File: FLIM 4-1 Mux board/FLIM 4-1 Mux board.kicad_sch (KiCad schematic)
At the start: 17 parts, among them U1 PTMUX8109PWR, U2 DI79L18UAB, U3 DI78L18UAB

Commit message: Add buttons
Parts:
- added J1, J2: Conn_01x14_Pin, symbol Connector:Conn_01x14_Pin
- added J3: Conn_01x05_Pin, symbol Connector:Conn_01x05_Pin
- added R3: 1k, Resistor_SMD:R_0805_2012Metric, symbol Device:R
- added SW1: SW_Push_LED, Custom:TSSLE 6868 R RNN J, symbol Switch:SW_Push_LED
- added U4: Itsy_Bitsy_32u4, Custom:Itsy Bitsy 32u4 with headers, symbol custom:Itsy_Bitsy_32u4
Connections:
- net GND: now also J1.4 (Pin_4), J2.2 (Pin_2), J3.2 (Pin_2), SW1.1, SW1.3 (K), U4.16 (Gnd), U4.32 (Gnd), U4.4 (GND)
- new net: R3.1, SW1.4 (A)
- new net 3v3: J1.14 (Pin_14), U4.14 (3.3V)
- new net 5V: J1.2 (Pin_2), U4.2 (5V)
- no-connect marks 0 -> 10

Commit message: Last update before change to cascade RF switches
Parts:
- added R4, R5, R6: 1k, Resistor_SMD:R_0805_2012Metric, symbol Device:R
- added SW2, SW3, SW4: SW_Push_LED, Custom:TSSLE 6868 R RNN J, symbol Switch:SW_Push_LED
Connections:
- net GND: now also SW2.1, SW2.3 (K), SW3.1, SW3.3 (K), SW4.1, SW4.3 (K)
- new net: R4.1, SW2.4 (A)
- new net: R5.1, SW3.4 (A)
- new net: R6.1, SW4.4 (A)
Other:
- moved on the sheet: R3, SW1

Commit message: Working draft of full setup
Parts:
- removed PS1: PDSE1-S24-D24-M, PDSE1-S24-D24-M:CONV_PDSE1-S24-D24-M, symbol Custom:PDSE1-S24-D24-M
- removed R1, R2, R3, R4, R5, R6: 1k, Resistor_SMD:R_0805_2012Metric, symbol Device:R
- removed U1: PTMUX8109PWR, TSSOP_8109PWR_TEX, symbol Custom:PTMUX8109PWR
- removed U2: DI79L18UAB, Package_TO_SOT_SMD:SOT-89-3, symbol Regulator_Linear:MCP1703Ax-150xxMB
- removed U3: DI78L18UAB, Package_TO_SOT_SMD:SOT-89-3, symbol Regulator_Linear:MCP1804x-1802xDB
- added C12, C13, C14: 8.2 nF, Capacitor_SMD:C_0402_1005Metric, symbol Device:C_Small
- added C15, C16, C17, C18, C19, C20: 100 pF, Capacitor_SMD:C_0603_1608Metric, symbol Device:C_Small
- added C21, C22, C23, C24: 1 µF, Capacitor_SMD:C_0603_1608Metric, symbol Device:C_Small
- added J10, J11, J12, J13: Conn_01x03_Socket, Connector_PinSocket_2.54mm:PinSocket_1x03_P2.54mm_Vertical_SMD_Pin1Left, symbol Connector:Conn_01x03_Socket
- added J14, J15, J16, J17: Conn_01x03_Pin, symbol Connector:Conn_01x03_Pin
- added J4, J5, J6, J7, J8: Conn_Coaxial, Custom:60312242114510, symbol Connector:Conn_Coaxial
- added J9: Barrel_Jack, Custom:CONN4_00165_TEN, symbol Connector:Barrel_Jack
- added R1, R10, R11, R12, R2, R3, R4, R5, R6, R7, R8, R9: 1k, Resistor_SMD:R_0603_1608Metric, symbol Device:R_Small
- added U1, U5, U6: SPDT RF switch, Custom:MSOP8G_8_ADI, symbol Custom:HMC284AMS8GETR
- added U2: CD74HCT175M96, Custom:74HCT175, symbol Custom:CD74HCT175M96
- added U3: ADM7150ARDZ-5.0, Custom:ADM7150ARDZ-5, symbol Custom:ADM7150ARDZ-5.0
- C1, C3: value 10µF -> 8.2 nF; footprint Capacitor_SMD:C_0805_2012Metric -> Capacitor_SMD:C_0402_1005Metric; Manufacturer Cal-Chip Electronics, Inc. -> Murata Electronics; Part # GMC21X5R106K50NT -> GRM1555C1H822GE01D
- C10, C11: value 100nF -> 1 µF; footprint Capacitor_SMD:C_0805_2012Metric -> Capacitor_SMD:C_0603_1608Metric; Manufacturer Cal-Chip Electronics, Inc. -> Walsin Technology Corporation; Part # GMC21X7R104M100NT -> 0603B105K250CT
- C2, C4: value 100nF -> 8.2 nF; footprint Capacitor_SMD:C_0805_2012Metric -> Capacitor_SMD:C_0402_1005Metric; Manufacturer Cal-Chip Electronics, Inc. -> Murata Electronics; Part # GMC21X7R104M100NT -> GRM1555C1H822GE01D
- C5: value 4.7µF -> 10 µF; footprint Capacitor_SMD:C_0805_2012Metric -> Capacitor_SMD:C_1210_3225Metric; Manufacturer Murata Electronics -> Walsin Technology Corporation; Part # GRM21BR71C475KE51L -> 1210B106M500CT
- C6, C7: value 470nF -> 10 µF; footprint Capacitor_SMD:C_0805_2012Metric -> Capacitor_SMD:C_1210_3225Metric; Manufacturer Samsung Electro-Mechanics -> Walsin Technology Corporation; Part # CL21B474KBFNNNG -> 1210B106M500CT
- C8, C9: value 470nF -> 1 µF; footprint Capacitor_SMD:C_0805_2012Metric -> Capacitor_SMD:C_0603_1608Metric; Manufacturer Samsung Electro-Mechanics -> Walsin Technology Corporation; Part # CL21B474KBFNNNG -> 0603B105K250CT
- SW1, SW2, SW3, SW4: footprint Custom:TSSLE 6868 R RNN J -> (none); Manufacturer Knitter-Switch -> Same Sky (Formerly CUI Devices); Part # TSSLE 6868 R RNN J -> PB4L-M-RR-D-67
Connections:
- net +24V is gone; now on net GND: C6.1
- net +5V is gone; now on net GND: C5.1
- net -24V is gone; now on net GND: C7.2
- net GND: now also C10.1, C8.2, C15.2, C16.2, C17.2, C18.2, C19.2, C20.2, C21.2, C22.2, C23.2, C24.2, J10.3 (Pin_3), J11.3 (Pin_3), J12.3 (Pin_3), J13.3 (Pin_3), J14.3 (Pin_3), J15.3 (Pin_3), J16.3 (Pin_3), J17.3 (Pin_3), J4.2 (Ext), J5.2 (Ext), J6.2 (Ext), J7.2 (Ext), J8.2 (Ext), J9.2, R2.1, U1.6 (GND), U1.7 (GND), U1.9 (EPAD), U2.13 (D3), U2.8 (GND), U3.4 (GND), U3.EPAD, U5.6 (GND), U5.7 (GND), U5.9 (EPAD), U6.6 (GND), U6.7 (GND), U6.9 (EPAD); no longer C1.1, C10.2, C2.1, C3.1, C4.1, C5.2, C6.2, C7.1, C8.1
- net at SW1.2: now also J14.1 (Pin_1)
- net at SW1.4 (A): now also J14.2 (Pin_2)
- net at SW2.4 (A): now also J15.2 (Pin_2)
- net at SW3.4 (A): now also J16.2 (Pin_2)
- net at SW3.2: now also J16.1 (Pin_1)
- net at SW2.2: now also J15.1 (Pin_1)
- net at SW4.4 (A): now also J17.2 (Pin_2)
- net at C9.1: now also U3.5 (REF_SENSE), U3.6 (REF)
- net at SW4.2: now also J17.1 (Pin_1)
- net LED1: now reaches U4.20 (0_RX)
- net LED1: now also R9.1
- net LED2: now reaches U4.21 (1_TX)
- net LED2: now also R10.1
- net LED3: now reaches U4.22 (2_SDA)
- net LED3: now also R11.1
- net LED4: now reaches U4.23 (~3_SCL)
- net LED4: now also R12.1
- net CLK: now reaches U4.26 (~9_A9)
- net CLK: now also R2.2, U2.9 (CP)
- net D1: now reaches U4.27 (~10_A10)
- net D1: now also U2.4 (D0)
- net D2: now reaches U4.28 (~11)
- net D2: now also U2.5 (D1)
- net D3: now reaches U4.29 (12_A11)
- net D3: now also U2.12 (D2)
- net +12V: now reaches U4.33 (VBat)
- net +12V: now also C6.2, J2.1 (Pin_1), J9.1, U3.7 (EN), U3.8 (VIN)
- net Button1: now reaches U4.5 (18_A0)
- net Button1: now also J10.1 (Pin_1)
- net Button2: now reaches U4.6 (19_A1)
- net Button2: now also J11.1 (Pin_1)
- net Button3: now reaches U4.7 (20_A2)
- net Button3: now also J12.1 (Pin_1)
- net Button4: now reaches U4.8 (21_A3)
- net Button4: now also J13.1 (Pin_1)
- removed net +18V: C1.2, C10.1, C2.2
- removed net -18V: C11.2, C3.2, C4.2
- new net: C24.1, J13.2 (Pin_2), R12.2
- new net: C21.1, J10.2 (Pin_2), R9.2
- new net: C22.1, J11.2 (Pin_2), R10.2
- new net: C8.1, U3.3 (BYP)
- new net: C13.1, J8.1 (In)
- new net: C13.2, U1.8 (RF2)
- new net: C5.2, U3.1 (VREG)
- new net: C10.2, R1.2, U2.1 (*MR)
- new net: C12.1, J6.1 (In)
- new net: C23.1, J12.2 (Pin_2), R11.2
- new net: C12.2, U6.3 (RFC)
- new net: C1.1, J4.1 (In)
- new net: C1.2, U5.8 (RF2)
- new net: C3.2, U6.5 (RF1)
- new net: C4.1, U6.8 (RF2)
- new net: C2.1, J5.1 (In)
- new net: C2.2, U5.5 (RF1)
- new net: C4.2, U1.3 (RFC)
- new net: C14.2, U1.5 (RF1)
- new net: C14.1, J7.1 (In)
- new net: C3.1, U5.3 (RFC)
- new net +5VA: C11.2, C7.1, R1.1, U2.16 (VCC), U3.2 (VOUT)
- new net A1: R3.1, U2.2 (Q0)
- new net A1*: C15.1, R3.2, U5.1 (A)
- new net A2: R5.1, U2.7 (Q1)
- new net A2*: C17.1, R5.2, U1.1 (A)
- new net A3: R7.1, U2.10 (Q2)
- new net A3*: C19.1, R7.2, U6.1 (A)
- new net B1: R4.1, U2.3 (*Q0)
- new net B1*: C16.1, R4.2, U5.2 (B)
- new net B2: R6.1, U2.6 (*Q1)
- new net B2*: C18.1, R6.2, U1.2 (B)
- new net B3: R8.1, U2.11 (*Q2)
- new net B3*: C20.1, R8.2, U6.2 (B)
- no-connect marks 10 -> 12
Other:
- note added: "Drill 12 mm hole"
- moved on the sheet: J1, J2, J3, U4

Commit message: non islated DC jack with filter
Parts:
- added C25: 100 µF, Capacitor_SMD:CP_Elec_10x10, symbol Device:C_Polarized_US
- added C26, C27, C29: 1 µF, Capacitor_SMD:C_0603_1608Metric, symbol Device:C_Small
- added C28: 10 µF, Capacitor_SMD:C_1210_3225Metric, symbol Device:C_Small
- added D1: TVS, Package_TO_SOT_SMD:SOT-23, symbol Device:D_Zener_Dual_CommonCathode_AAK
- added D2: D_Schottky, Diode_SMD:D_SOD-323, symbol Device:D_Schottky
- added FB1: FerriteBead_Small, Inductor_SMD:L_0603_1608Metric, symbol Device:FerriteBead_Small
- added FL1: Choke_CommonMode_PulseElectronics_PH9455x105NL, Custom:WE-SL2, symbol Filter:Choke_CommonMode_PulseElectronics_PH9455x105NL
- added J18: Conn_01x02_Socket, `, symbol Connector:Conn_01x02_Socket
- added J19: Conn_01x02_Pin, Custom:SAMTEC_TSM-102-02-L-SH, symbol Connector:Conn_01x02_Pin
- added R13: 100, Resistor_SMD:R_0805_2012Metric, symbol Device:R_Small
- J9: footprint Custom:CONN4_00165_TEN -> `; Manufacturer Tensility International Corp -> Switchcraft Inc.; Part # 54-00165 -> 712AFMS
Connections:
- net +12V: now also D1.1 (A), D2.2 (A), J18.1 (Pin_1), J19.1 (Pin_1); no longer C6.2, U3.7 (EN), U3.8 (VIN)
- net GND: now also C25.2, C26.2, C29.2, FL1.3; no longer J9.2
- new net: C29.1, FB1.1, FL1.4
- new net: C27.1, C28.1, D2.1 (K), FL1.1
- new net: FB1.2, R13.1
- new net +12VA: C25.1, C26.1, C6.2, R13.2, U3.7 (EN), U3.8 (VIN)
- new net GNDPWR: C27.2, C28.2, D1.2 (A), FL1.2, J18.2 (Pin_2), J19.2 (Pin_2), J9.2
- no-connect marks 12 -> 13
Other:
- moved on the sheet: C5, C6, C7, C8, C9, J9, U3

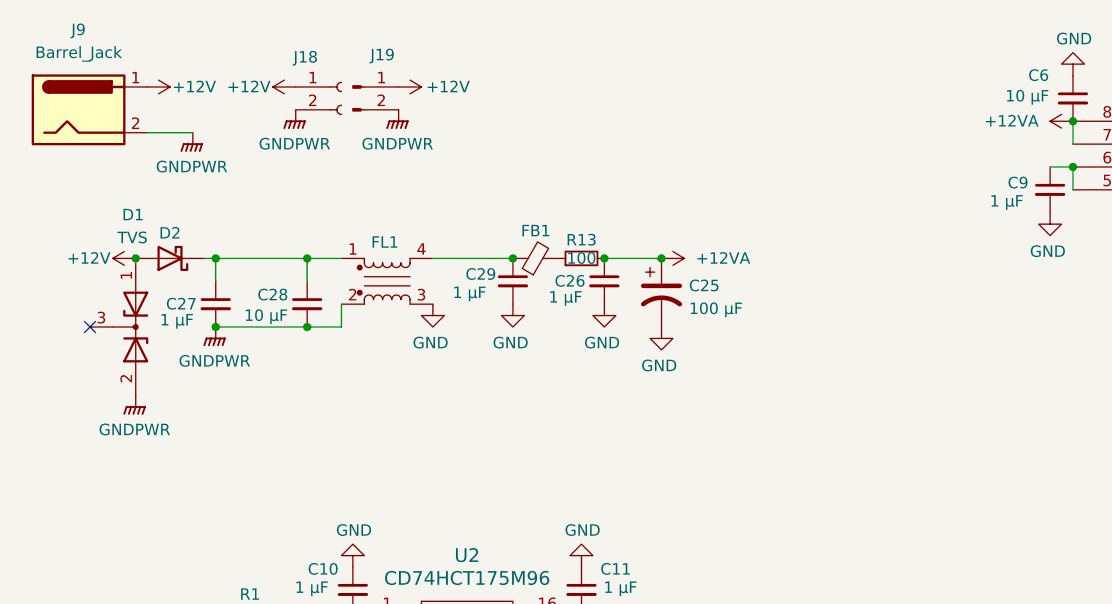
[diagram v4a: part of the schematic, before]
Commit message: Improved filtering with isolated dirty DC before common choke
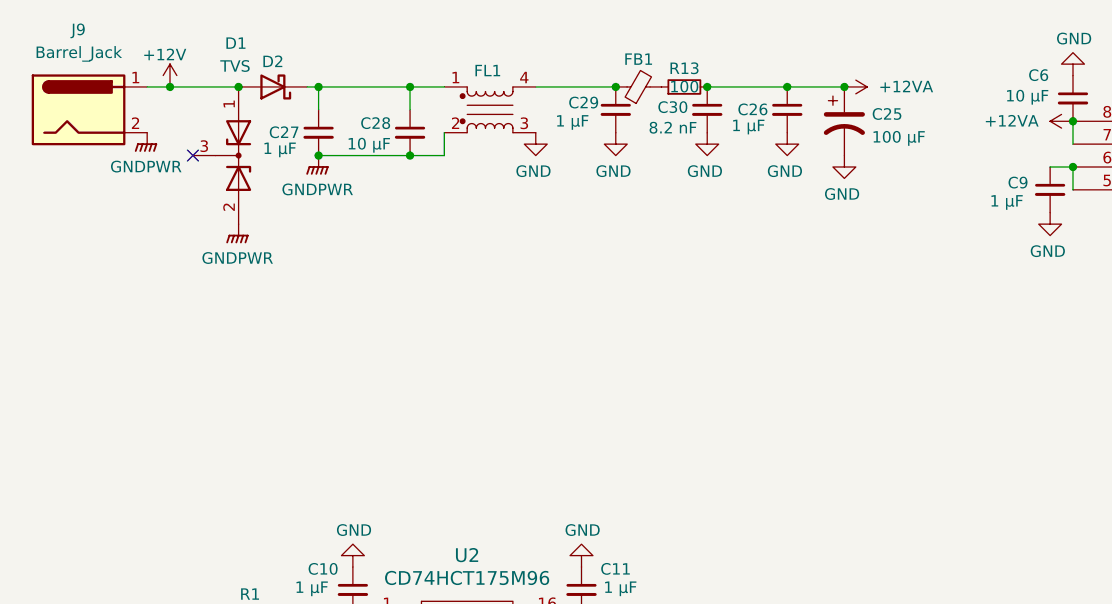
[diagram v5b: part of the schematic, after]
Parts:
- removed J18: Conn_01x02_Socket, `, symbol Connector:Conn_01x02_Socket
- removed J19: Conn_01x02_Pin, Custom:SAMTEC_TSM-102-02-L-SH, symbol Connector:Conn_01x02_Pin
- added C30: 8.2 nF, Capacitor_SMD:C_0402_1005Metric, symbol Device:C_Small
- C10, C11, C21, C22, C23, C24, C26, C27, C29, C8, C9: footprint Capacitor_SMD:C_0603_1608Metric -> Capacitor_SMD:C_0805_2012Metric; Part # 0603B105K250CT -> 0805B105K500CT
- J9: footprint ` -> Custom:CONN4_00165_TEN; Manufacturer Switchcraft Inc. -> Tensility; Part # 712AFMS -> 54-00165
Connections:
- net +12VA: now also C30.1
- net GND: now also C30.2
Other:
- moved on the sheet: C25, C26, C27, C28, C29, D1, D2, FB1, FL1, R13

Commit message: Design notes added
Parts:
- added R14, R15, R16: 1k, Resistor_SMD:R_0603_1608Metric, symbol Device:R_Small
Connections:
- net D1: now also R15.2
- net D2: now also R14.2
- net D3: now also R16.2
- net GND: now also R14.1, R15.1, R16.1
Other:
- note added: "Add pulldown resistor at input the schmitt trigger, and 10k to D1-D3 to allow cable to be disconnected. - ACASA100121002P100"
- note added: "Add schmitt trigger SN74LVC1G17 to CLK at ethernet jack, and RC filters (1k + 8.2 nF) to D1-D3 at the ethernet jack"

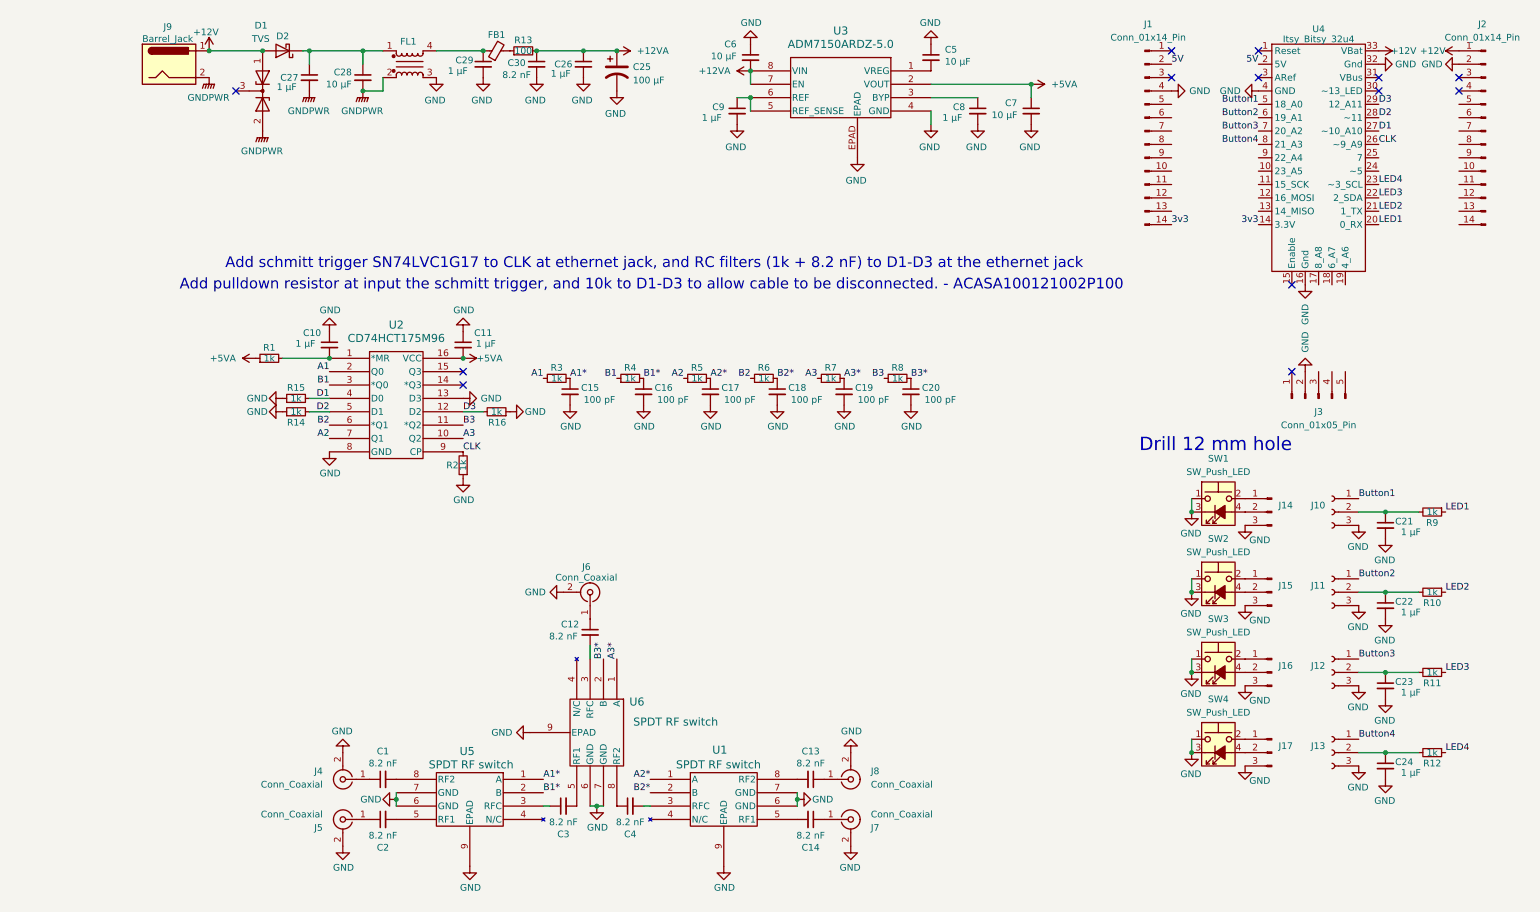
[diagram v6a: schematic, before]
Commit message: Add PTC fuse, fix minor issues
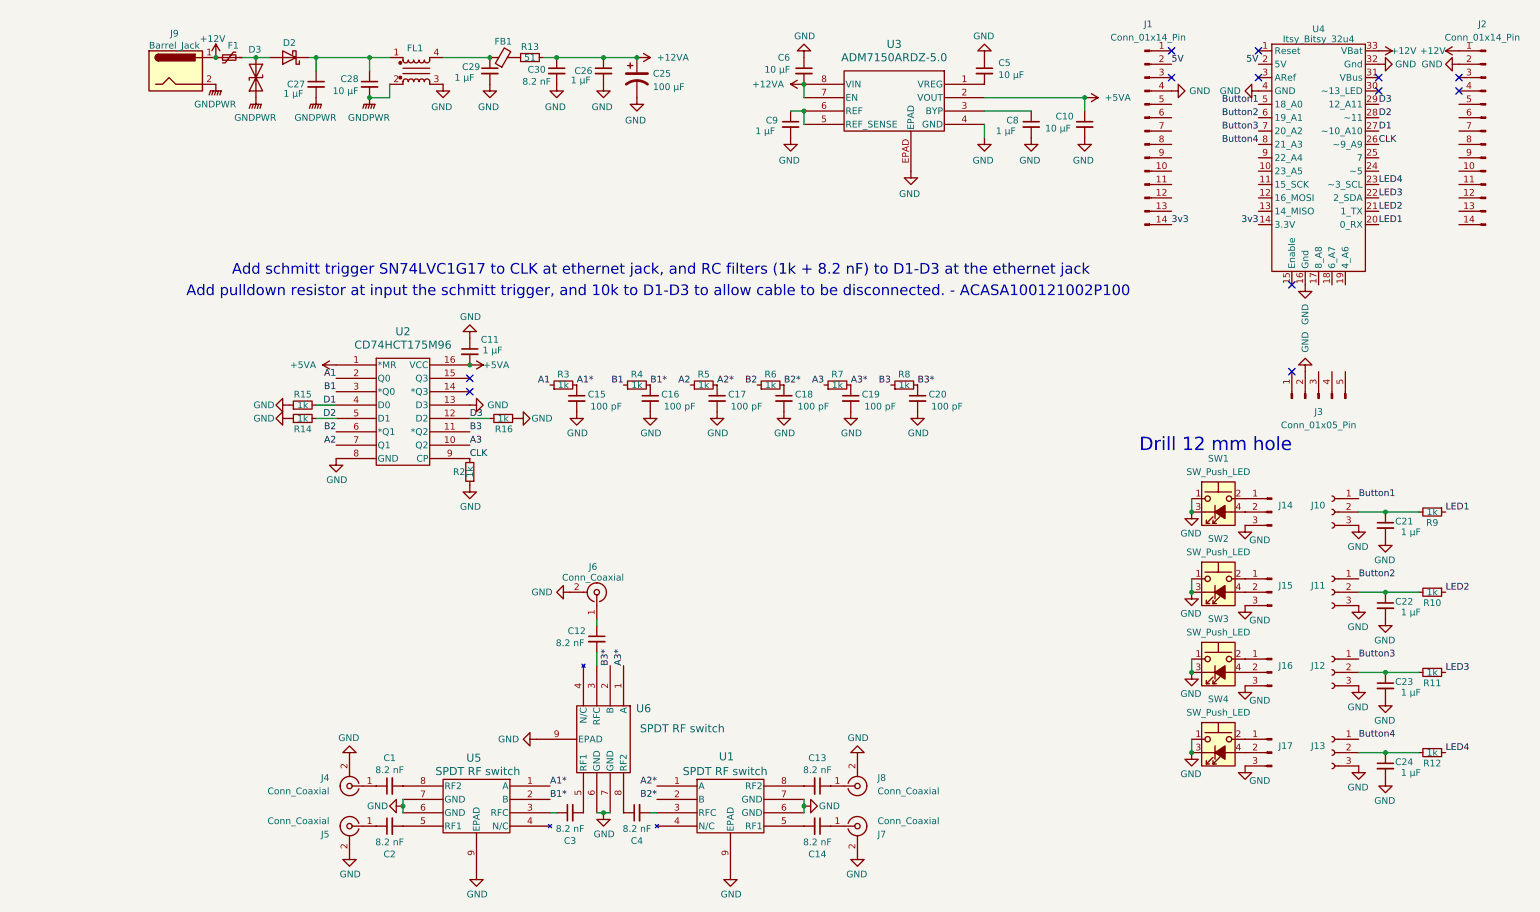
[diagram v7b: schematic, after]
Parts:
- removed C7: 10 µF, Capacitor_SMD:C_1210_3225Metric, symbol Device:C_Small
- removed D1: TVS, Package_TO_SOT_SMD:SOT-23, symbol Device:D_Zener_Dual_CommonCathode_AAK
- removed R1: 1k, Resistor_SMD:R_0603_1608Metric, symbol Device:R_Small
- added D3: SMAJ13CA, Diode_SMD:D_SMA, symbol Diode:SMAJ13CA
- added F1: Polyfuse_Small, Fuse:Fuse_0603_1608Metric, symbol Device:Polyfuse_Small
- C10: value 1 µF -> 10 µF; footprint Capacitor_SMD:C_0805_2012Metric -> Capacitor_SMD:C_1210_3225Metric; Part # 0805B105K500CT -> 1210B106M500CT
- FL1: value Choke_CommonMode_PulseElectronics_PH9455x105NL -> choke
- R13: value 100 -> 51; Part # TNPW0805100RFEEA -> TNPW080551R0BEEA
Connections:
- net +12V: now also F1.1; no longer D2.2 (A)
- net +5VA: now also C10.1, U2.1 (*MR)
- net GND: now also C10.2; no longer C10.1
- net GNDPWR: now also D3.2 (A2)
- new net: D2.2 (A), D3.1 (A1), F1.2
- no-connect marks 13 -> 12
